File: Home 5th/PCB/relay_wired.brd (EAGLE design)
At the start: 100 x 80 mm, 9 parts, among them K1 G5Q-1-EU DC12

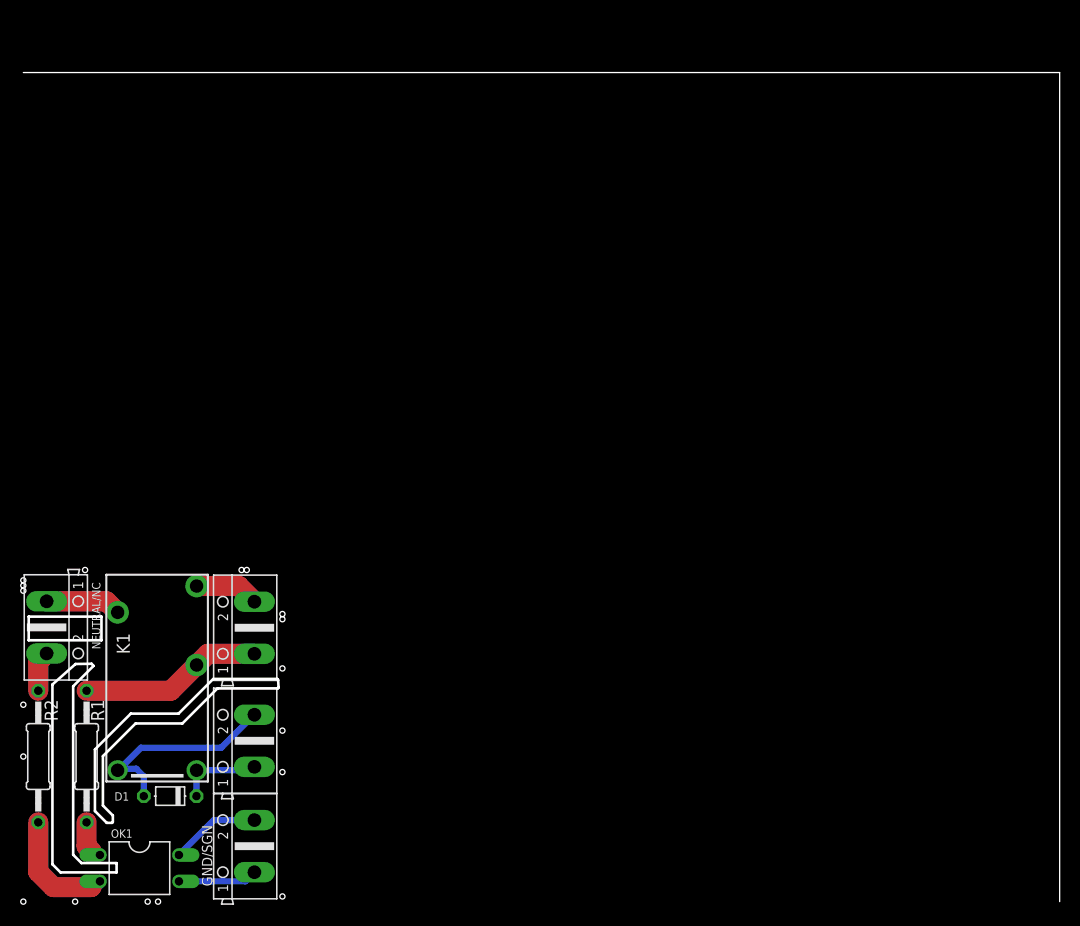
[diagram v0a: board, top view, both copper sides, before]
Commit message: Adding and removing some Drill holes
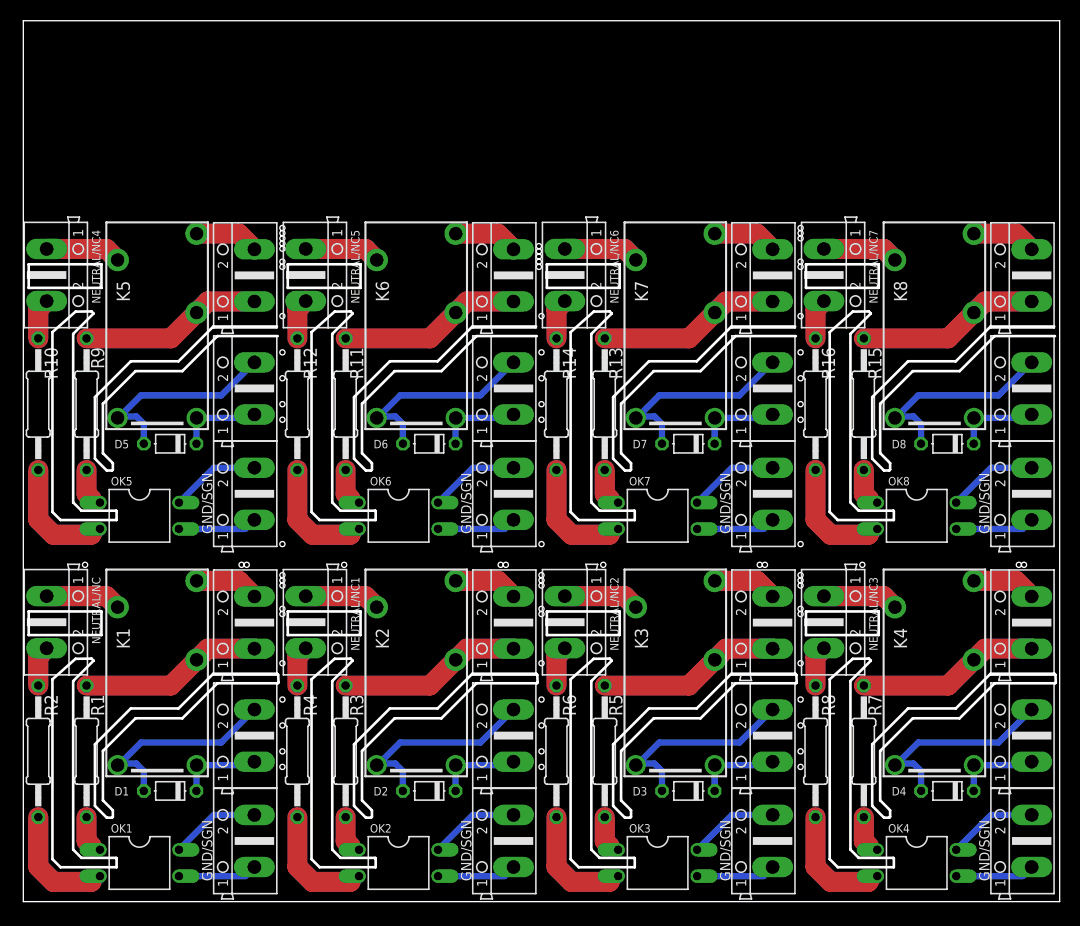
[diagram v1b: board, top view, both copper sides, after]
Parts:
- added D2, D3, D4, D5, D6, D7, D8: 1N4007, diode:D-5
- added GND/S1, GND/S2, GND/S3, GND/S4, GND/S5, GND/S6, GND/S7, LOAD/NO1, LOAD/NO2, LOAD/NO3, LOAD/NO4, LOAD/NO5, LOAD/NO6, LOAD/NO7, NEUTRAL/NC1, NEUTRAL/NC2, NEUTRAL/NC3, NEUTRAL/NC4, NEUTRAL/NC5, NEUTRAL/NC6, NEUTRAL/NC7, VEXT/BJT1, VEXT/BJT2, VEXT/BJT3, VEXT/BJT4, VEXT/BJT5, VEXT/BJT6, VEXT/BJT7: (no value), con-ptr500-modified:AK500/2
- added K2, K3, K4, K5, K6, K7, K8: G5Q-1-EU DC12, relay:G5SB
- added OK2, OK3, OK4, OK5, OK6, OK7, OK8: SFH620A, optocoupler:DIL04
- added R10, R11, R12, R13, R14, R15, R16, R3, R4, R5, R6, R7, R8, R9: 22k/2W, rcl:0207/12
- moved D1 0.50 mm to (14.2, 10.7)
- moved GND/S 0.50 mm to (22.3, 5.85)
- moved K1 0.50 mm to (12.9, 20.8)
- moved LOAD/NO 0.50 mm to (22.3, 26.9)
- moved NEUTRAL/NC 0.50 mm to (2.25, 27.0)
- moved OK1 0.50 mm to (11.2, 3.73)
- moved R1 0.50 mm to (6.11, 14.5)
- moved R2 0.50 mm to (1.44, 14.5)
- moved VEXT/BJT 0.50 mm to (22.3, 16.0)
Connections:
- new net N$1: K5.2, LOAD/NO4.1, R9.1
- new net N$10: D5.C, K5.1, VEXT/BJT4.1
- new net N$11: D5.A, K5.5, VEXT/BJT4.2
- new net N$13: K5.3, LOAD/NO4.2
- new net N$14: GND/S4.2, OK5.4
- new net N$15: GND/S4.1, OK5.3
- new net N$16: K6.2, LOAD/NO5.1, R11.1
- new net N$17: NEUTRAL/NC5.2, R12.1
- new net N$18: K6.4, NEUTRAL/NC5.1
- new net N$19: OK6.2, R12.2
- new net N$2: NEUTRAL/NC4.2, R10.1
- new net N$20: OK6.1, R11.2
- new net N$21: D6.C, K6.1, VEXT/BJT5.1
- new net N$22: D6.A, K6.5, VEXT/BJT5.2
- new net N$23: K6.3, LOAD/NO5.2
- new net N$24: GND/S5.2, OK6.4
- new net N$26: GND/S5.1, OK6.3
- new net N$27: K7.2, LOAD/NO6.1, R13.1
- new net N$28: NEUTRAL/NC6.2, R14.1
- new net N$29: K7.4, NEUTRAL/NC6.1
- new net N$3: K5.4, NEUTRAL/NC4.1
- new net N$34: K2.2, LOAD/NO1.1, R3.1
- new net N$35: NEUTRAL/NC1.2, R4.1
- new net N$36: K2.4, NEUTRAL/NC1.1
- new net N$37: OK2.2, R4.2
- new net N$38: OK2.1, R3.2
- new net N$39: D2.C, K2.1, VEXT/BJT1.1
- new net N$4: OK5.2, R10.2
- new net N$40: D2.A, K2.5, VEXT/BJT1.2
- new net N$41: K2.3, LOAD/NO1.2
- new net N$42: GND/S1.2, OK2.4
- new net N$43: GND/S1.1, OK2.3
- new net N$44: K3.2, LOAD/NO2.1, R5.1
- new net N$45: NEUTRAL/NC2.2, R6.1
- new net N$46: K3.4, NEUTRAL/NC2.1
- new net N$47: OK3.2, R6.2
- new net N$48: OK3.1, R5.2
- new net N$49: D3.C, K3.1, VEXT/BJT2.1
- new net N$50: D3.A, K3.5, VEXT/BJT2.2
- new net N$51: K3.3, LOAD/NO2.2
- new net N$52: GND/S2.2, OK3.4
- new net N$53: GND/S2.1, OK3.3
- new net N$54: K4.2, LOAD/NO3.1, R7.1
- new net N$55: NEUTRAL/NC3.2, R8.1
- new net N$56: K4.4, NEUTRAL/NC3.1
- new net N$57: OK4.2, R8.2
- new net N$58: OK4.1, R7.2
- new net N$59: D4.C, K4.1, VEXT/BJT3.1
- new net N$60: D4.A, K4.5, VEXT/BJT3.2
- new net N$61: K4.3, LOAD/NO3.2
- new net N$62: GND/S3.2, OK4.4
- new net N$63: GND/S3.1, OK4.3
- new net N$64: OK7.2, R14.2
- new net N$65: OK7.1, R13.2
- new net N$66: D7.C, K7.1, VEXT/BJT6.1
- new net N$67: D7.A, K7.5, VEXT/BJT6.2
- new net N$68: K7.3, LOAD/NO6.2
- new net N$69: GND/S6.2, OK7.4
- new net N$70: GND/S6.1, OK7.3
- new net N$71: K8.2, LOAD/NO7.1, R15.1
- new net N$72: NEUTRAL/NC7.2, R16.1
- new net N$73: K8.4, NEUTRAL/NC7.1
- new net N$74: OK8.2, R16.2
- new net N$75: OK8.1, R15.2
- new net N$76: D8.C, K8.1, VEXT/BJT7.1
- new net N$77: D8.A, K8.5, VEXT/BJT7.2
- new net N$78: K8.3, LOAD/NO7.2
- new net N$79: GND/S7.2, OK8.4
- new net N$80: GND/S7.1, OK8.3
- new net N$9: OK5.1, R9.2
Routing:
- net N$1: track 0.00 -> 23.5 mm
- net N$44: track 0.00 -> 23.5 mm
- net N$27: track 0.00 -> 23.5 mm
- net N$34: track 0.00 -> 23.5 mm
- net N$71: track 0.00 -> 23.5 mm
- net N$54: track 0.00 -> 23.5 mm
- net N$16: track 0.00 -> 23.5 mm
- net N$74: track 0.00 -> 23.1 mm
- net N$64: track 0.00 -> 23.1 mm
- net N$57: track 0.00 -> 23.1 mm
- net N$4: track 0.00 -> 23.1 mm
- net N$19: track 0.00 -> 23.1 mm
- net N$37: track 0.00 -> 23.1 mm
- net N$47: track 0.00 -> 23.1 mm
- net N$11: track 0.00 -> 19.8 mm
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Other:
- board size 100 x 80 mm -> 100 x 85 mm
